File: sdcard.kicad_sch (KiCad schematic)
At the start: 20 parts, among them J9 microSD push-pull, Q2 -20V 2.3A P-ch, Q3 60V 300mA N-ch

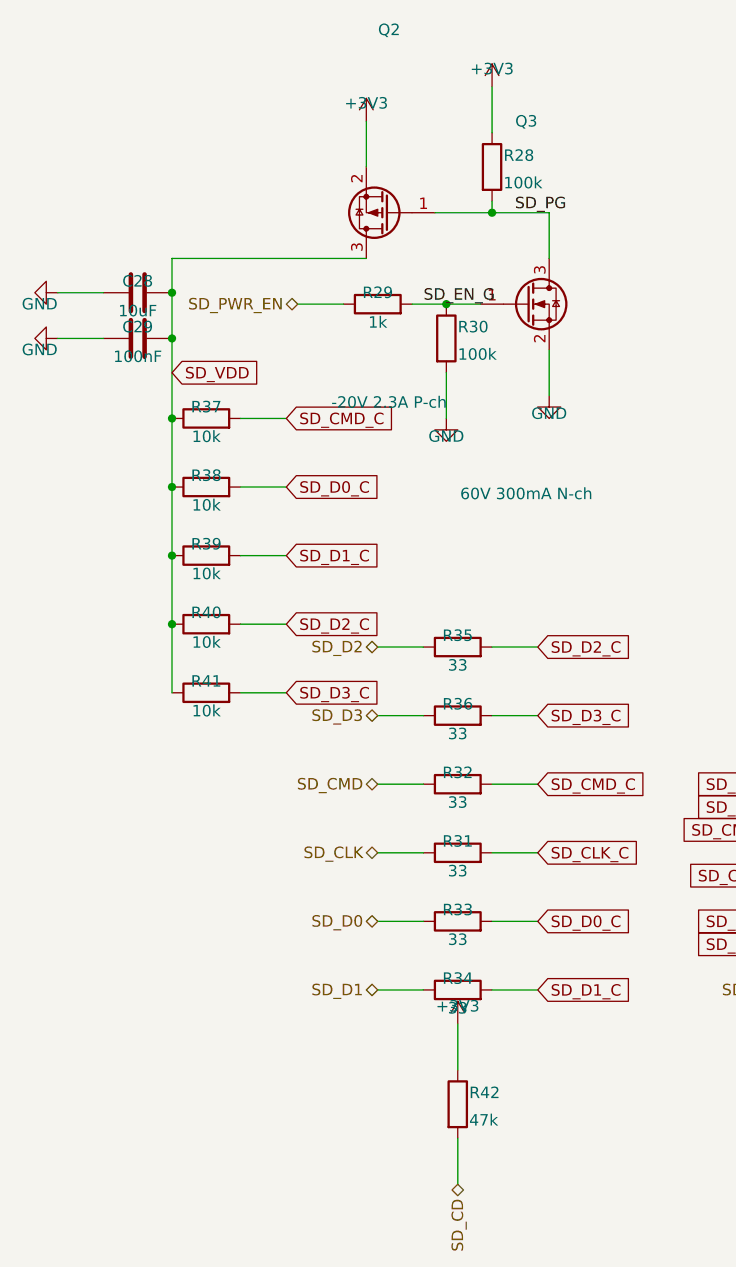
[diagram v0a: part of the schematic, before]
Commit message: Power-fail ride-through: detect, coast, shed; board grows to 84 x 100
The ignition cuts this board's power with a log file open, every drive.
Three new pieces make that survivable, all simulated before layout:

- Detect: TLV431 + 100k/12.7k divider on VBAT_F, AHEAD of the ideal
  diode, asserting PWR_FAIL (IO15) at 11.0 V with ~0.3 V hysteresis.
  The harness collapses microseconds after the key turns while +VBAT
  coasts, so the warning costs no stored energy.
- Coast: two 220 uF/100 V cans join the 100 uF on +VBAT. 540 uF on the
  input rail, where a volt of headroom is worth most.
- Shed: AO3401 + 2N7002 high-side switch on the sensor rail (SENS_EN,
  IO16, off at reset), with PF1 moved behind it so a tripped sensor
  fuse can also be power-cycled from firmware.

Simulated end to end: detection <1 ms after the cut, then 108 ms to
converter dropout with sensors shed, 53 ms without -- the switch doubles
the flush budget. ISO pulse 1's brownout shortens from 8.2 to 5.6 ms.

The two cans plus the detector had no free board left on 84 x 84, so the
board grows to 84 x 100 (still JLC's cheap tier): bottom-edge furniture
and mounting holes move down 16 mm, one can per side, and the detector/
switch column gets its own placement zone. Also included from the audit:
the 3V3 buck's own input capacitor pair at its VIN pin (it was reaching
12.6 mm across to the 5 V island's), the CAN transceiver and AHCT buffer
bypasses pinned at their pins, and Power-class tracks at 0.55 mm to clear
IPC-2221 for 2 A at a 20 C rise.

Hard-won generator fix: a literal newline inside a symbol property is
accepted by KiCad's loader but silently breaks connectivity for every
symbol after it in the file -- the netlist dropped 45 components with no
error pointing anywhere near the cause. The emitter now flattens all
whitespace in property strings.

Board: 0 DRC violations, 0 unconnected, physical audit clean end to end.
185 components, 111 nets, ERC clean, netlist verified node-for-node.

Co-Authore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
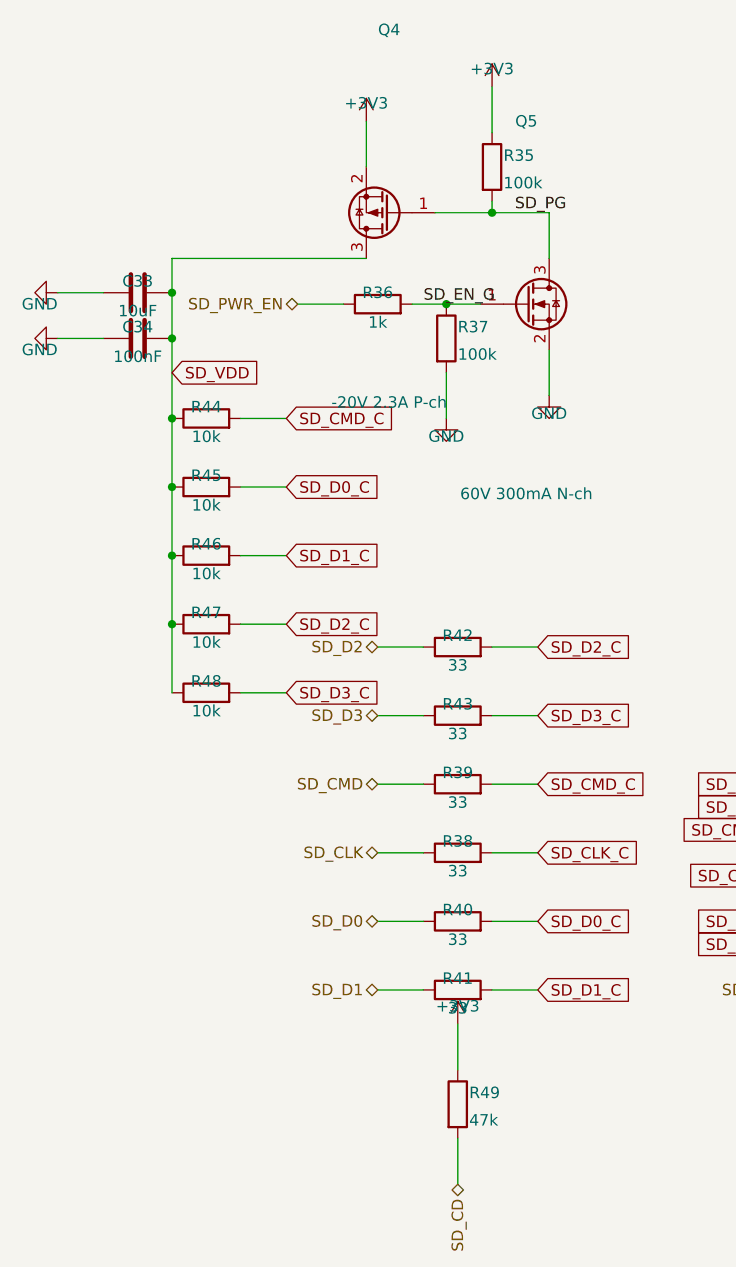
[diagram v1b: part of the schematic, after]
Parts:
- removed C28: 10uF, Capacitor_SMD:C_1206_3216Metric, symbol Device:C
- removed C29: 100nF, Capacitor_SMD:C_0805_2012Metric, symbol Device:C
- removed Q2: -20V 2.3A P-ch, Package_TO_SOT_SMD:SOT-23, symbol Transistor_FET:Q_PMOS_GSD
- removed Q3: 60V 300mA N-ch, Package_TO_SOT_SMD:SOT-23, symbol Transistor_FET:Q_NMOS_GSD
- removed R28, R30: 100k, Resistor_SMD:R_0805_2012Metric, symbol Device:R
- removed R29: 1k, Resistor_SMD:R_0805_2012Metric, symbol Device:R
- removed R31, R32, R33, R34: 33, Resistor_SMD:R_0805_2012Metric, symbol Device:R
- added C33: 10uF, Capacitor_SMD:C_1206_3216Metric, symbol Device:C
- added C34: 100nF, Capacitor_SMD:C_0805_2012Metric, symbol Device:C
- added Q4: -20V 2.3A P-ch, Package_TO_SOT_SMD:SOT-23, symbol Transistor_FET:Q_PMOS_GSD
- added Q5: 60V 300mA N-ch, Package_TO_SOT_SMD:SOT-23, symbol Transistor_FET:Q_NMOS_GSD
- added R43: 33, Resistor_SMD:R_0805_2012Metric, symbol Device:R
- added R44, R45, R46, R47, R48: 10k, Resistor_SMD:R_0805_2012Metric, symbol Device:R
- added R49: 47k, Resistor_SMD:R_0805_2012Metric, symbol Device:R
- R35: value 33 -> 100k; Note Series damping -> Default off
- R36: value 33 -> 1k; Note Series damping -> Series gate resistor. 10k here divided against R27 100k and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
- R37: value 10k -> 100k; Note Espressif's recommended value; pulled to the switched rail 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 -> (none)
- R38, R39, R40, R41: value 10k -> 33; Note Espressif's recommended value; pulled to the switched rail 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 -> Series damping
- R42: value 47k -> 33; Note Card-detect pull-up -> Series damping
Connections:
- net +3V3: now also R35.1, Q4.2 (S), R49.1; no longer R42.1
- net GND: now also R37.2, C33.2, C34.2, Q5.2 (S)
- net SD_CD: now also R49.2; no longer R42.2
- net SD_CLK: now also R38.1
- net SD_CLK_C: now also R38.2
- net SD_CMD: now also R39.1
- net SD_CMD_C: now also R39.2, R44.2; no longer R37.2
- net SD_D0: now also R40.1
- net SD_D0_C: now also R40.2, R45.2; no longer R38.2
- net SD_D1: now also R41.1
- net SD_D1_C: now also R41.2, R46.2; no longer R39.2
- net SD_D2: now also R42.1; no longer R35.1
- net SD_D2_C: now also R42.2, R47.2; no longer R35.2, R40.2
- net SD_D3: now also R43.1; no longer R36.1
- net SD_D3_C: now also R43.2, R48.2; no longer R36.2, R41.2
- net SD_EN_G: now also R36.2, R37.1, Q5.1 (G)
- net SD_PG: now also R35.2, Q4.1 (G), Q5.3 (D)
- net SD_PWR_EN: now also R36.1
- net SD_VDD: now also C33.1, C34.1, Q4.3 (D), R44.1, R45.1, R46.1, R47.1, R48.1; no longer R37.1, R38.1, R39.1, R40.1, R41.1
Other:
- moved on the sheet: R35, R36, R37, R38, R39, R40, R41, R42

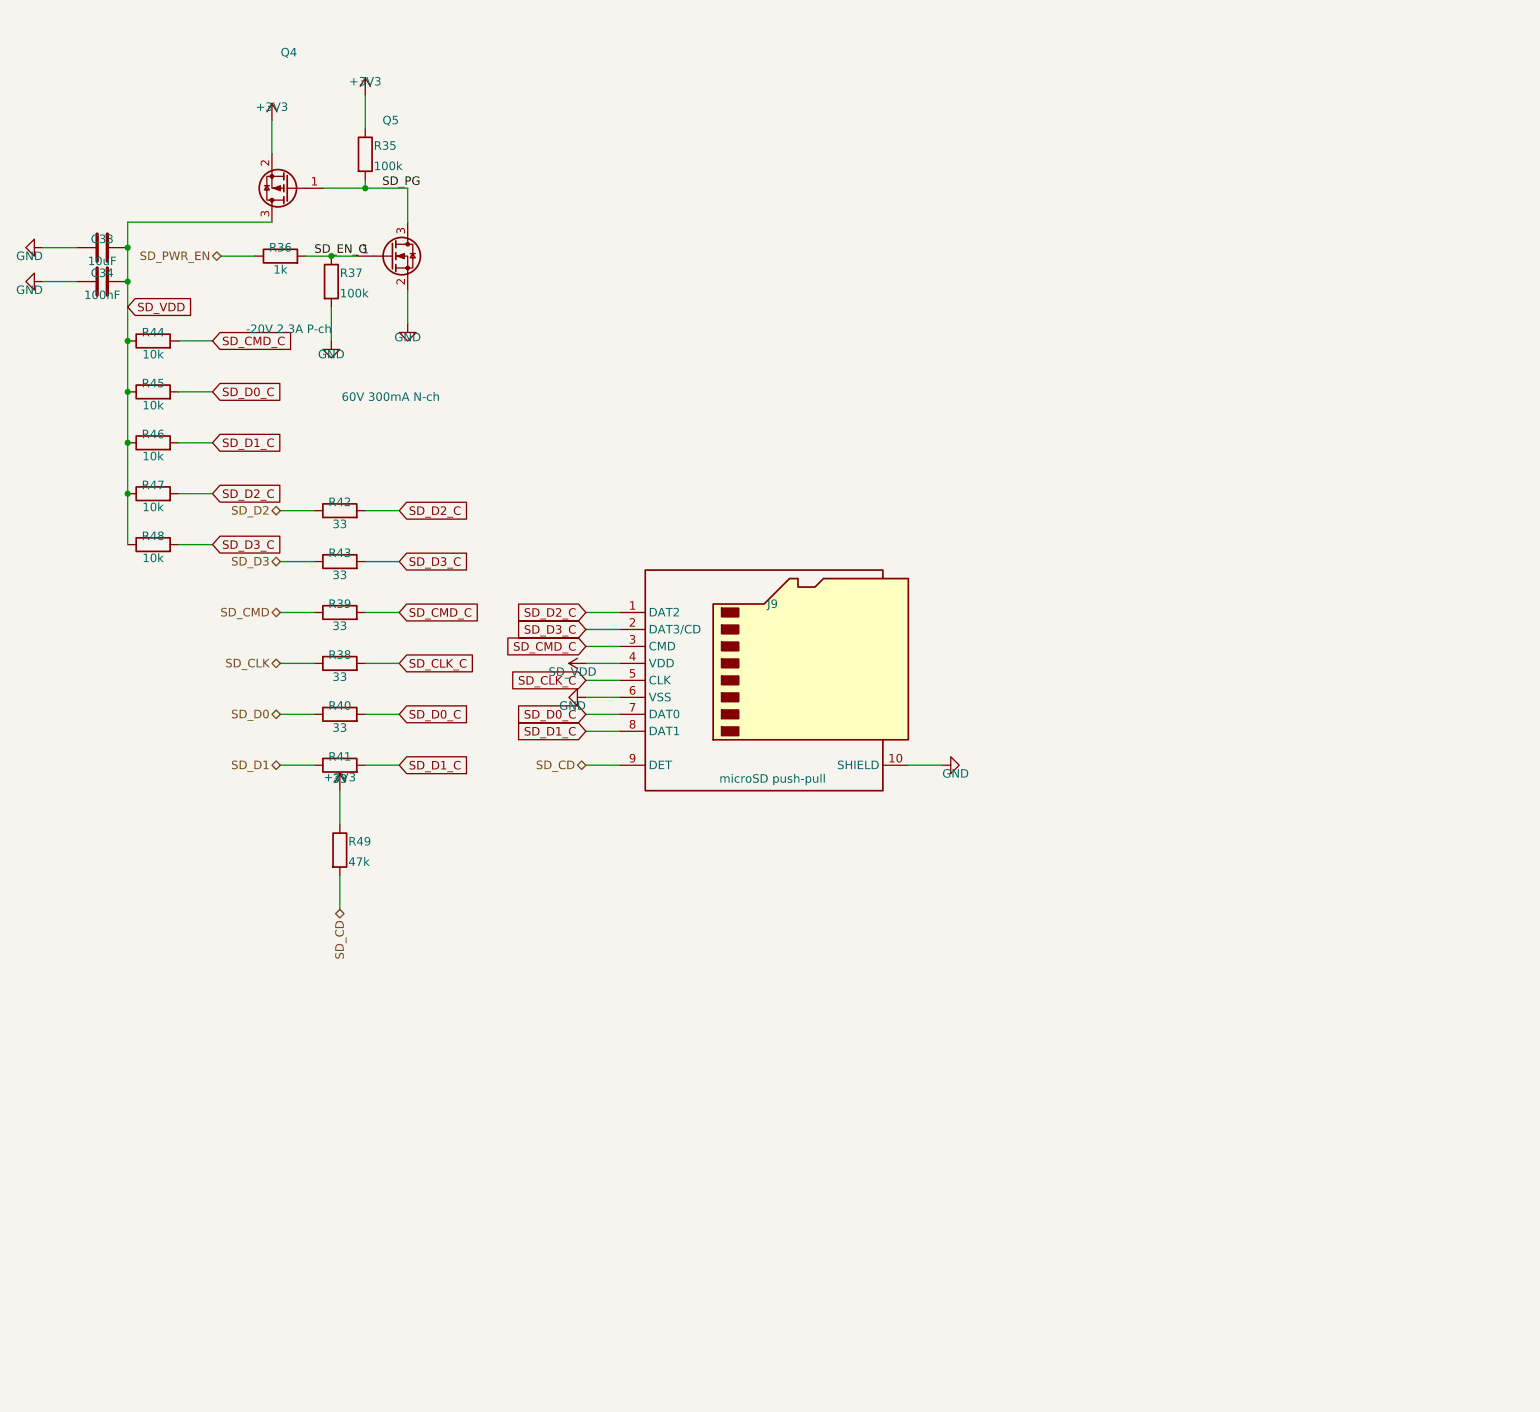
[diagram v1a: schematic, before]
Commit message: USB OVP, card-slot ESD, SD test points, and a gold-standard schematic
Hardware, all simulation- or review-driven:
- USB overvoltage cutoff: TLV431 + AO3401 + MMBT3906 series switch on
  VBUS, tripping at 5.77 V. Re-simulated: a compliant 5 V source passes
  at 4.99 V, the switch opens at 5.95 V of brick, and the +5V rail never
  exceeds 5.2 V from anything up to 14 V -- where a 9 V brick previously
  drove it to 8.4 V against the TJA1051's 6 V absolute maximum.
  Off-the-shelf OVP parts were rejected first: the TPS25200 class cuts
  off near 7 V, which is no protection for a 6 V limit.
- Two SRV05-4 arrays clamp every microSD card contact (LCSC C13612);
  until now the ESP32's ~2 kV pin diodes were all that stood behind a
  card swapped by hand after every session.
- A second USBLC6 clamps the USB-C CC pins -- the first contacts every
  plug insertion touches, previously landing on bare 5.1k resistors.
- Test points on SD_CLK and SD_CMD, the most likely scope targets at
  bring-up and otherwise reachable only on fine-pitch pads.

The schematic itself was rebuilt to read like a reference design
(RejsaCAN was the benchmark): every circuit is now a hand-drawn block --
power-fail detector, sensor-rail switch, USB OVP, connector pull-
resistor clusters, and a single utility panel for test points, ERC
flags, mounting holes and the power LED. Sentence-length values became
part numbers ("0.2A PTC", "AO3401A", "600R") with ratings kept in
hidden fields, which also answers the external review's value-hygiene
findings. Title blocks carry rev B and a date. The Power sheet shrank
from A2 back to A3 in the process.

gen/README.md now documents the whole pipeline -- stages, the block-
drawing conventions with per-rotation pin geometry, the junction rules,
and the traps (property newlines, off-grid points, anchors keeping
their natural rotation) -- so the next board reuses all of it.

Board: 84 x 100, 0 DRC violations, 0 unconnected, 0 courtyard overlaps,
physical audit clean. BOM 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
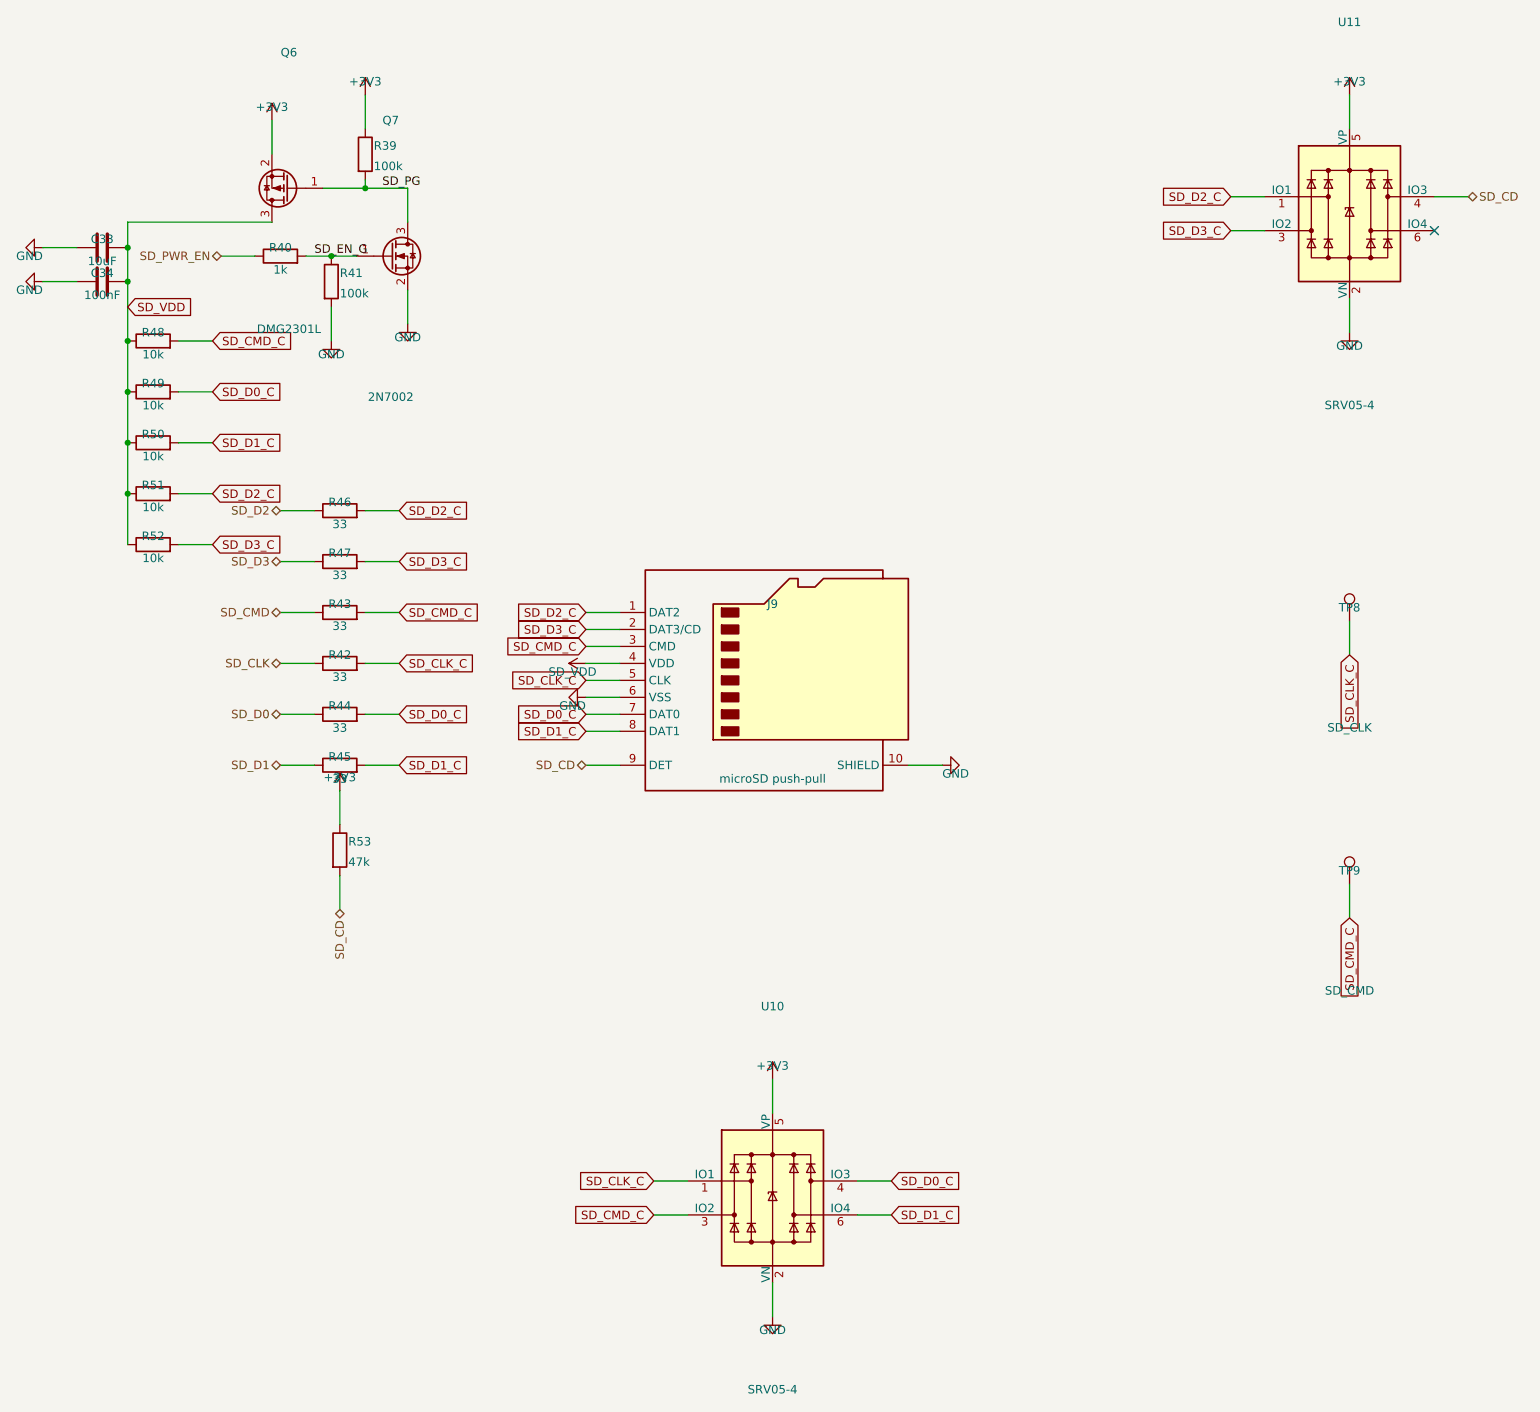
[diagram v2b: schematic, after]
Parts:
- removed Q4: -20V 2.3A P-ch, Package_TO_SOT_SMD:SOT-23, symbol Transistor_FET:Q_PMOS_GSD
- removed Q5: 60V 300mA N-ch, Package_TO_SOT_SMD:SOT-23, symbol Transistor_FET:Q_NMOS_GSD
- removed R35, R37: 100k, Resistor_SMD:R_0805_2012Metric, symbol Device:R
- removed R36: 1k, Resistor_SMD:R_0805_2012Metric, symbol Device:R
- removed R38: 33, Resistor_SMD:R_0805_2012Metric, symbol Device:R
- added Q6: DMG2301L, Package_TO_SOT_SMD:SOT-23, symbol Transistor_FET:Q_PMOS_GSD
- added Q7: 2N7002, Package_TO_SOT_SMD:SOT-23, symbol Transistor_FET:Q_NMOS_GSD
- added R50, R51, R52: 10k, Resistor_SMD:R_0805_2012Metric, symbol Device:R
- added R53: 47k, Resistor_SMD:R_0805_2012Metric, symbol Device:R
- added TP8: SD_CLK, TestPoint:TestPoint_Pad_D1.5mm, symbol Connector:TestPoint
- added TP9: SD_CMD, TestPoint:TestPoint_Pad_D1.5mm, symbol Connector:TestPoint
- added U10, U11: SRV05-4, Package_TO_SOT_SMD:SOT-23-6, symbol Power_Protection:SRV05-4
- R39: value 33 -> 100k; Note Series damping -> Default off
- R40: value 33 -> 1k; Note Series damping -> Series gate resistor. 10k here divided against R27 100k and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
- R41: value 33 -> 100k; Note Series damping -> (none)
- R44, R45, R46, R47: value 10k -> 33; Note Espressif's recommended value; pulled to the switched rail 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 -> Series damping
- R49: value 47k -> 10k; Note Card-detect pull-up -> Espressif's recommended value; pulled to the switched rail 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
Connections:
- net +3V3: now also R39.1, Q6.2 (S), R53.1, U10.5 (VP), U11.5 (VP); no longer R49.1
- net GND: now also R41.2, Q7.2 (S), U10.2 (VN), U11.2 (VN)
- net SD_CD: now also R53.2, U11.4 (IO3); no longer R49.2
- net SD_CLK: now also R42.1
- net SD_CLK_C: now also R42.2, TP8.1, U10.1 (IO1)
- net SD_CMD: now also R43.1; no longer R39.1
- net SD_CMD_C: now also R43.2, R48.2, TP9.1, U10.3 (IO2); no longer R39.2, R44.2
- net SD_D0: now also R44.1; no longer R40.1
- net SD_D0_C: now also R44.2, R49.2, U10.4 (IO3); no longer R40.2, R45.2
- net SD_D1: now also R45.1; no longer R41.1
- net SD_D1_C: now also R45.2, R50.2, U10.6 (IO4); no longer R41.2, R46.2
- net SD_D2: now also R46.1; no longer R42.1
- net SD_D2_C: now also R46.2, R51.2, U11.1 (IO1); no longer R42.2, R47.2
- net SD_D3: now also R47.1; no longer R43.1
- net SD_D3_C: now also R47.2, R52.2, U11.3 (IO2); no longer R43.2, R48.2
- net SD_EN_G: now also R40.2, R41.1, Q7.1 (G)
- net SD_PG: now also R39.2, Q6.1 (G), Q7.3 (D)
- net SD_PWR_EN: now also R40.1
- net SD_VDD: now also R49.1, Q6.3 (D), R50.1, R51.1, R52.1; no longer R44.1, R45.1, R46.1, R47.1
- no-connect marks 0 -> 1
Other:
- moved on the sheet: R39, R40, R41, R42, R43, R44, R45, R46, R47, R48, R49
